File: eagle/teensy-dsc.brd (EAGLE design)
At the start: 76.6 x 51.2 mm, 27 parts, among them J1 RJ11-6PTH, J2 RJ11-6PTH, J3 RJ45-8PTH, J4 POWER_JACKPTH, M1 XBEERX-VN, Q1 IRLML6344, X1 STEREOJACK, X2 STEREOJACK

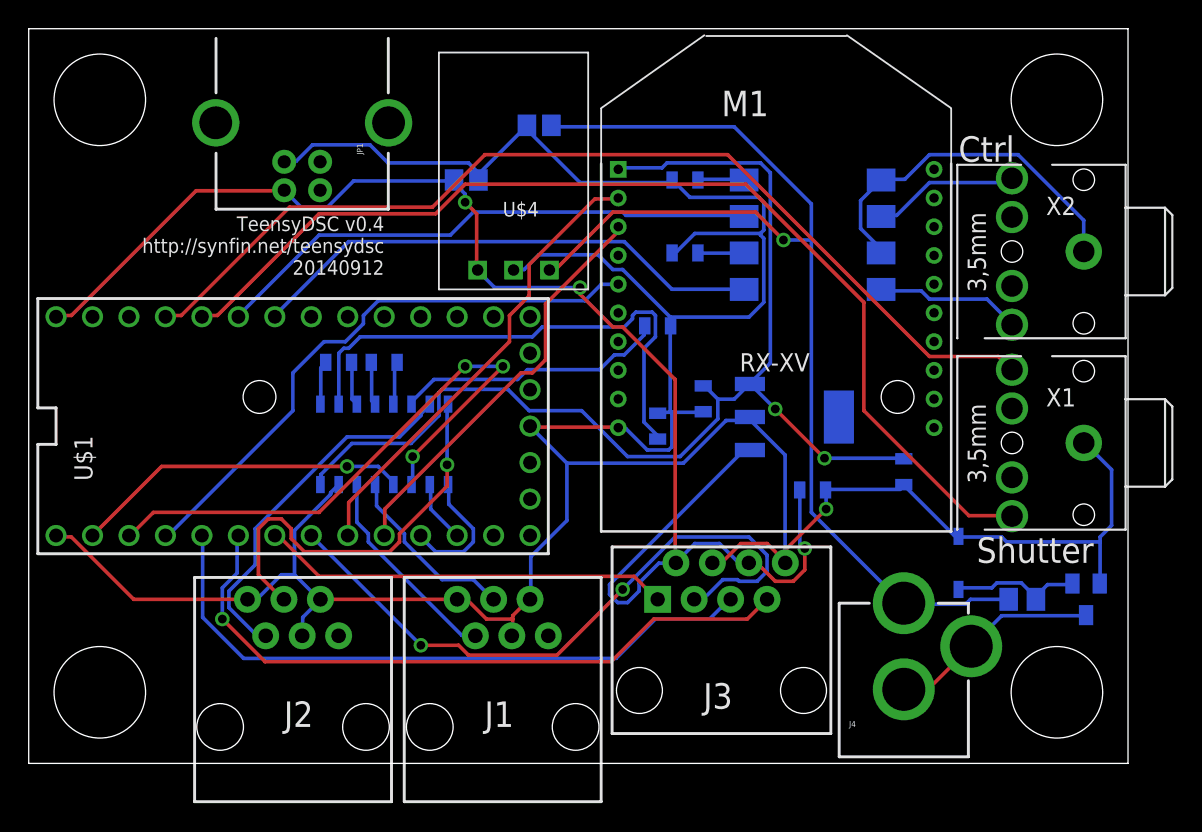
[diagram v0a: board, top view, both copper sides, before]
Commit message: v0.5 simple board/just DSC functionality
No serial, camera, etc.
Has USB & 12V power input options
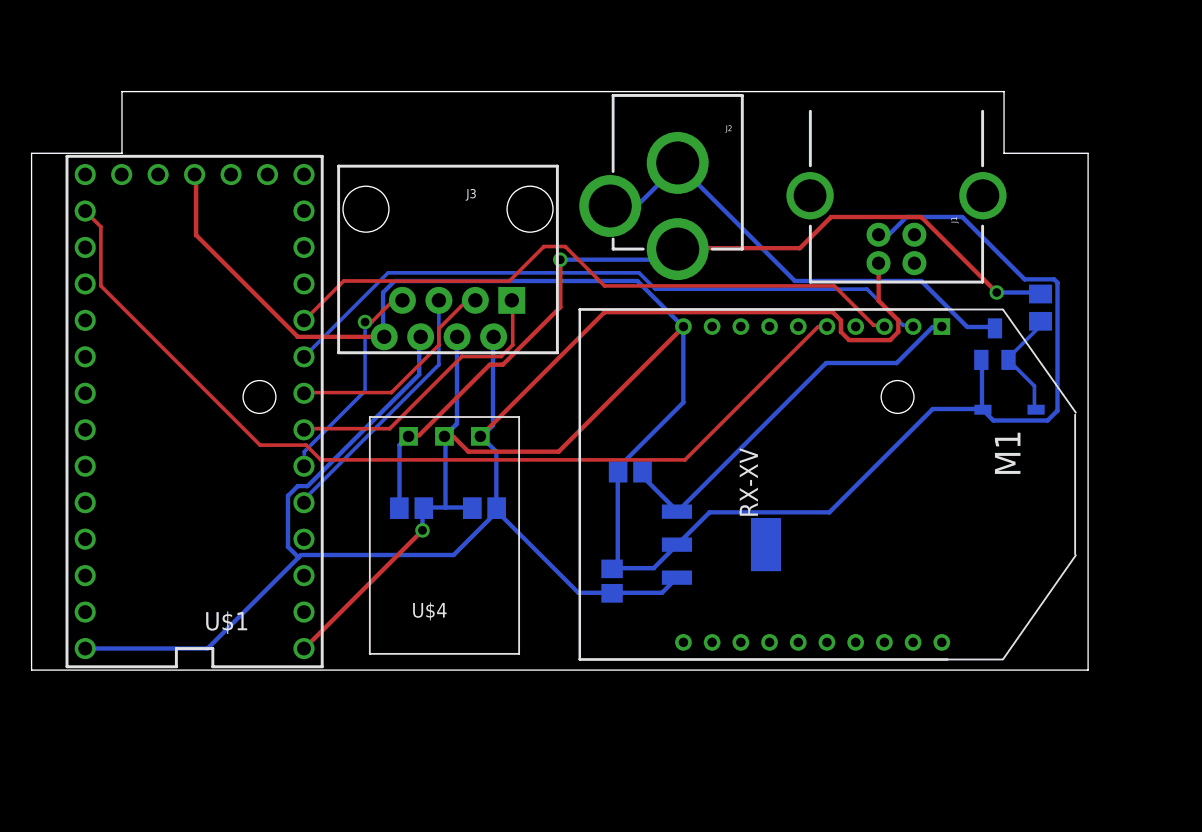
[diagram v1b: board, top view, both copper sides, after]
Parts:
- removed C3, C4, C5, C6, C7: 0.1uF, SparkFun-Passives:0805
- removed J4: POWER_JACKPTH, SparkFun-Connectors:POWER_JACK_PTH
- removed JP1: USB-B, SparkFun-Connectors:USB-B-PTH
- removed OK1: LTV826S, optocoupler:DIL8-SMD
- removed R1, R2: 470, SparkFun-Resistors:0805
- removed U$2: MAX3232IDW, SparkFun-DigitalIC:SO016
- removed X1, X2: STEREOJACK, adafruit:STX3100
- C1, C2: device SparkFun-Capacitors:0805 -> resistor:C0805
- J1: value RJ11-6PTH -> USB-B; device SparkFun-Connectors:RJ11-6 -> SparkFun-Connectors:USB-B-PTH
- J2: value RJ11-6PTH -> POWER_JACKPTH; device SparkFun-Connectors:RJ11-6 -> SparkFun-Connectors:POWER_JACK_PTH
- moved J2 56.8 mm to (45.2, 49.5), turned to 180 degrees
- moved J1 47.3 mm to (60.5, 36.8), turned to 270 degrees
- moved J3 38.6 mm to (29.2, 38.6), turned to 180 degrees
- moved C8 28.1 mm to (26.7, 17.8), turned to 180 degrees
- moved C9 22.9 mm to (31.8, 17.8), turned to 0 degrees
- moved R15 20.4 mm to (70.5, 31.8), turned to 90 degrees
- moved C1 19.1 mm to (41.9, 20.3), turned to 0 degrees
- moved Q1 18.9 mm to (67.3, 29.2), turned to 0 degrees
- moved C2 15.3 mm to (40.6, 12.7), turned to 90 degrees
- moved M1 14.3 mm to (53.3, 16.9), turned to 270 degrees
- moved D5 11.2 mm to (68.3, 24.6), turned to 0 degrees
- moved U$4 10.5 mm to (34.2, 24.1), turned to 180 degrees
- moved U$3 10.2 mm to (48.3, 15.2)
- moved U$1 6.93 mm to (11.6, 24.5), turned to 180 degrees
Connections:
- removed net FOCUS: OK1.8, X2.2
- removed net FOCUS-CTL: OK1.1, U$1.20/A6
- removed net N$1: C4.1, U$2.1
- removed net N$2: C4.2, U$2.3
- removed net N$3: C3.1, U$2.4
- removed net N$4: C3.2, U$2.5
- removed net N$5: C7.1, U$2.6
- removed net N$6: C6.1, U$2.2
- removed net N$7: OK1.4, R2.2
- removed net N$9: OK1.2, R1.2
- removed net RS1-RX: J1.3, U$2.13
- removed net RS1-TX: J1.2, U$2.14
- removed net RS2-RX: J2.3, U$2.8
- removed net RS2-TX: J2.2, U$2.7
- removed net SERIAL1-RX: U$1.0, U$2.12
- removed net SERIAL1-TX: U$1.1, U$2.11
- removed net SERIAL2-RX: U$1.9, U$2.9
- removed net SERIAL2-TX: U$1.10, U$2.10
- removed net SHUTTER: OK1.6, X2.5
- removed net SHUTTER-CTL: OK1.3, U$1.21/A7
- removed net SHUTTER-GND: OK1.5, OK1.7, X2.1
- removed net SW1: U$1.22/A8, X1.2
- removed net SW2: U$1.23/A9, X1.5
- net +12V: now also J2.PWR; no longer J4.PWR
- net 3.3V: no longer C5.1, U$2.16
- net 5V: now also C2.1, J1.VBUS; no longer C2.2, JP1.VBUS
- net GND: now also C2.2, J1.GND; no longer C2.1, C5.2, C6.2, C7.2, J1.1, J1.4, J1.5, J2.1, J2.4, J2.5, JP1.GND, R1.1, R2.1, U$2.15, X1.1
- net GND_MAIN: now also J2.GND, J2.GNDBREAK; no longer J4.GND, J4.GNDBREAK
- net XBEE_RST: now also U$1.14/A0; no longer U$1.2
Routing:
- net SW1: track 74.3 -> 0.00 mm
- net SW2: track 69.9 -> 0.00 mm
- net GND: track 230.5 -> 178.4 mm
- net 3.3V: track 79.5 -> 27.6 mm, vias 2 -> 0
- net SERIAL1-TX: track 41.8 -> 0.00 mm, vias 3 -> 0
- net SHUTTER-CTL: track 38.5 -> 0.00 mm
- net N$6: track 36.4 -> 0.00 mm
- net FOCUS-CTL: track 36.3 -> 0.00 mm
- net CHAN-A-ALT/DEC: track 47.3 -> 15.0 mm
- net CHAN-A-AZ/RA: track 46.3 -> 15.3 mm, vias 2 -> 0
- net RS2-RX: track 28.4 -> 0.00 mm, vias 1 -> 0
- net CHAN-B-ALT/DEC: track 45.4 -> 18.0 mm
- net RS2-TX: track 25.5 -> 0.00 mm
- net SHUTTER-GND: track 25.2 -> 0.00 mm
- net XBEE_RST: track 40.8 -> 65.1 mm
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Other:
- board size 76.6 x 51.2 mm -> 73.6 x 40.3 mm
- board text added: "TeensyDSC v0.5 http://synfin.net/teensydsc 20141102"
- board text removed: "Ctrl"
- board text removed: "J1"
- board text removed: "J2"
- board text removed: "Shutter"
- board text removed: "TeensyDSC v0.4 http://synfin.net/teensydsc 20140912"

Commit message: Small improvements to simple board v0.5.1:
- Move RJ45 up to be flush with USB
- Move cap labels to be readable
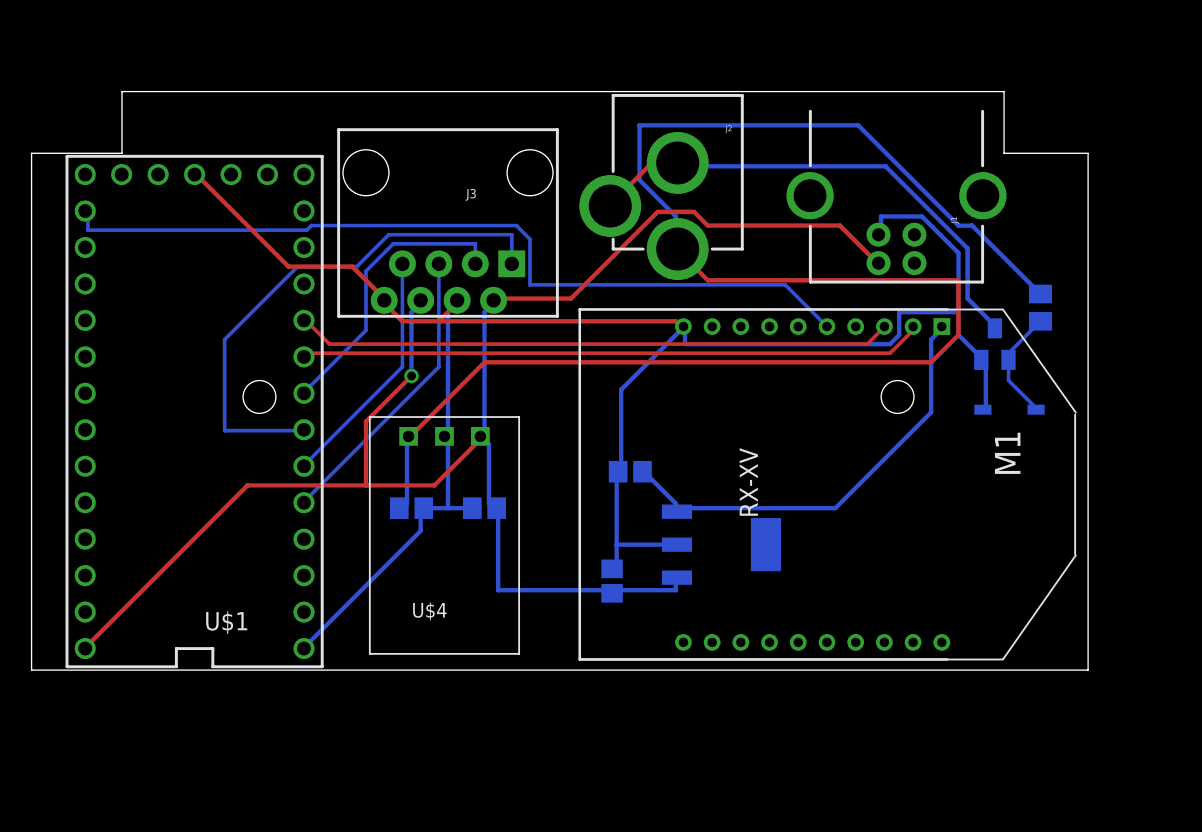
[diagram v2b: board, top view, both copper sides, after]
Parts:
- moved J3 2.54 mm to (29.2, 41.1)
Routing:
- net +12V: track 59.8 -> 113.5 mm, vias 2 -> 0
- net GND: track 178.4 -> 137.6 mm, vias 1 -> 0
- net CHAN-B-AZ/RA: track 20.2 -> 36.9 mm
- net XBEE_RST: track 65.1 -> 57.9 mm
- net 5V: track 120.8 -> 114.0 mm, vias 0 -> 1
- net CHAN-A-AZ/RA: track 15.3 -> 20.1 mm
- net XBEE_IN: track 44.9 -> 41.6 mm
- net 3.3V: track 27.6 -> 30.6 mm
- net XBEE_OUT: track 46.5 -> 43.5 mm
- net CHAN-B-ALT/DEC: track 18.0 -> 20.5 mm
- net GND_MAIN: track 32.9 -> 35.1 mm
- net CHAN-A-ALT/DEC: track 15.0 -> 16.9 mm, vias 1 -> 0
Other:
- board text added: "TeensyDSC v0.5.1 http://synfin.net/teensydsc 2014116"
- board text removed: "TeensyDSC v0.5 http://synfin.net/teensydsc 20141102"
